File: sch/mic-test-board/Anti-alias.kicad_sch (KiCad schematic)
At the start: 8 parts, among them J10 Mating pre-crimped connector,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, J7 Conn_01x04

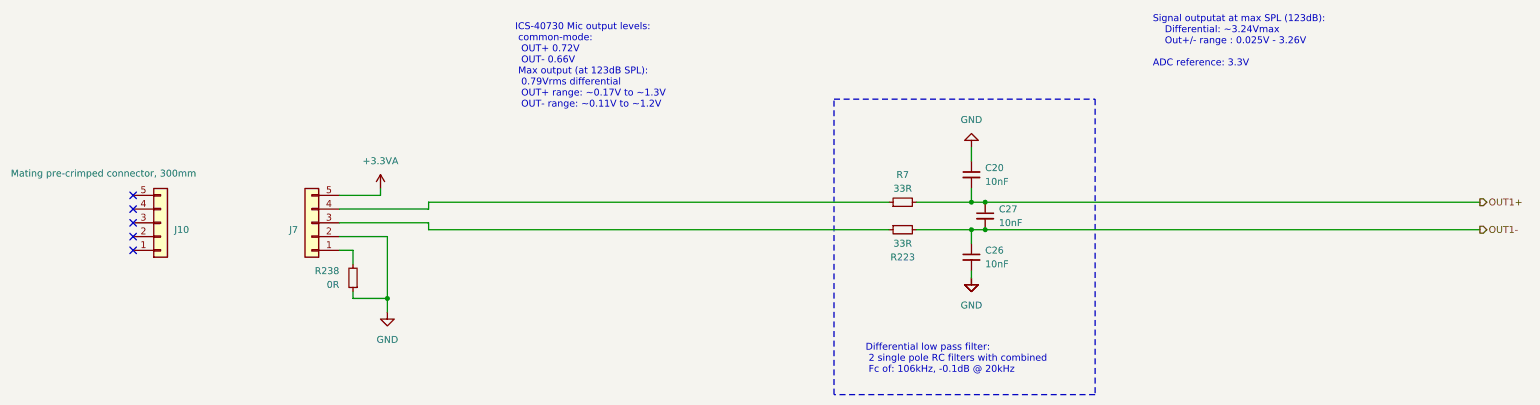
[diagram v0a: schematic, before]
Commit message: pcb: finished routing mic board and ADC board.
 - BOM complete
 - uController pinout configured with CubeMX and re-checked
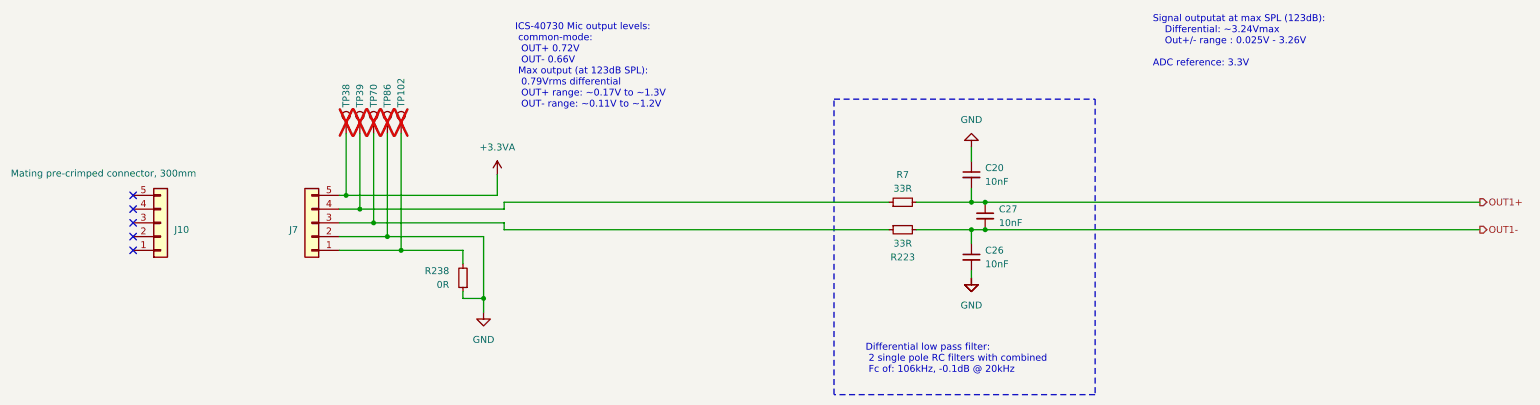
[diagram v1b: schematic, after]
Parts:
- added TP102, TP38, TP39, TP70, TP86: Hole_1.5mm, TestPoint:TestPoint_THTPad_D2.0mm_Drill1.0mm, symbol Connector:TestPoint
- C20, C26, C27: Manufacturer (none) -> KEMET; Part Number (none) -> C0603C103M4RAC7867; Supplier Number (none) -> 399-C0603C103M4RAC7867CT-ND; Voltage (none) -> 16V
- R223, R7: Manufacturer (none) -> Vishay Dale; Part Number (none) -> CRCW060333R0FKEAC; Supplier (none) -> Digi-Key; Supplier Number (none) -> 541-3988-1-ND
- R238: Manufacturer (none) -> Stackpole Electronics Inc; Part Number (none) -> RMCF0603ZT0R00; Supplier (none) -> Digi-Key; Supplier Number (none) -> RMCF0603ZT0R00CT-ND
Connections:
- net +3.3VA: now also TP38.1
- net GND: now also TP86.1
- net at J7.1 (Pin_1), R238.2: now also TP102.1
- net at J7.3 (Pin_3), R223.1: now also TP70.1
- net at J7.4 (Pin_4), R7.1: now also TP39.1
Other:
- moved on the sheet: R238

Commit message: pcb: ordered PCB's and BOM! RevA and v240506
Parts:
- J7: value Conn_01x04 -> Conn_01x05
- TP102, TP38, TP39, TP70, TP86: now fitted; now left out of the parts list
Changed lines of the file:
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@@
 			)
 		)
-		(property "Value" "Conn_01x04"
+		(property "Value" "Conn_01x05"
 			(at 97.79 142.2401 0)
 			(effects
@@
 		(unit 1)
 		(exclude_from_sim no)
-		(in_bom yes)
+		(in_bom no)
 		(on_board yes)
-		(dnp yes)
+		(dnp no)
 		(property "Reference" "TP102"
 			(at 116.84 122.174 90)
@@
 			)
 		)
-		(property "Supplier Number" ""
+		(property "Supplier Number" "~"
 			(at 116.84 127 0)
 			(effects
@@
 		(unit 1)
 		(exclude_from_sim no)
-		(in_bom yes)
+		(in_bom no)
 		(on_board yes)
-		(dnp yes)
+		(dnp no)
 		(property "Reference" "TP39"
 			(at 109.22 122.174 90)
@@
 			)
 		)
-		(property "Supplier Number" ""
+		(property "Supplier Number" "~"
 			(at 109.22 127 0)
 			(effects
@@
 		(unit 1)
 		(exclude_from_sim no)
-		(in_bom yes)
+		(in_bom no)
 		(on_board yes)
-		(dnp yes)
+		(dnp no)
 		(property "Reference" "TP38"
 			(at 106.68 122.174 90)
@@
 			)
 		)
-		(property "Supplier Number" ""
+		(property "Supplier Number" "~"
 			(at 106.68 127 0)
 			(effects
@@
 		(unit 1)
 		(exclude_from_sim no)
-		(in_bom yes)
+		(in_bom no)
 		(on_board yes)
-		(dnp yes)
+		(dnp no)
 		(property "Reference" "TP70"
 			(at 111.76 122.174 90)
@@
 			)
 		)
-		(property "Supplier Number" ""
+		(property "Supplier Number" "~"
 			(at 111.76 127 0)
 			(effects
@@
 		(unit 1)
 		(exclude_from_sim no)
-		(in_bom yes)
+		(in_bom no)
 		(on_board yes)
-		(dnp yes)
+		(dnp no)
 		(property "Reference" "TP86"
 			(at 114.3 122.174 90)
@@
 			)
 		)
-		(property "Supplier Number" ""
+		(property "Supplier Number" "~"
 			(at 114.3 127 0)
 			(effects
